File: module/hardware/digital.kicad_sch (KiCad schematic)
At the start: 41 parts, among them J10 Conn_01x03, J11 Conn_01x03, J12 Conn_01x03, J5 Conn_01x03_Male, J6 Conn_01x03_Male, J7 Conn_01x03, J8 Conn_01x03, J9 Conn_01x05_Male, SW2 SW_Push, U8 W25Q128JVS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

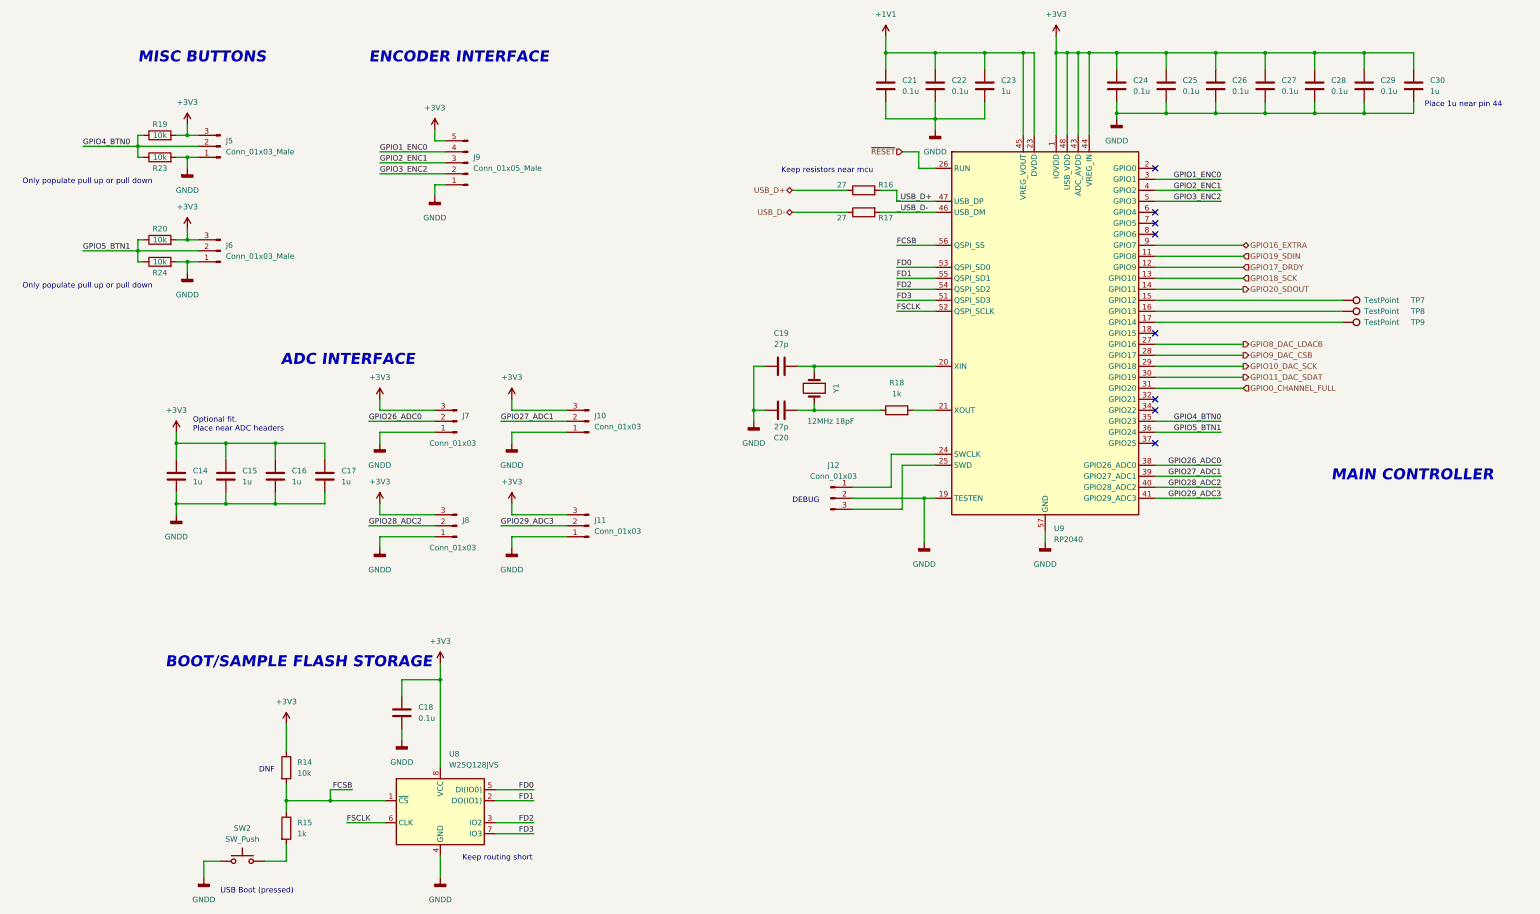
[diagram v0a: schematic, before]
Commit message: Add EXTRA1, btn debounce passives; Bump HW rev to 1.1
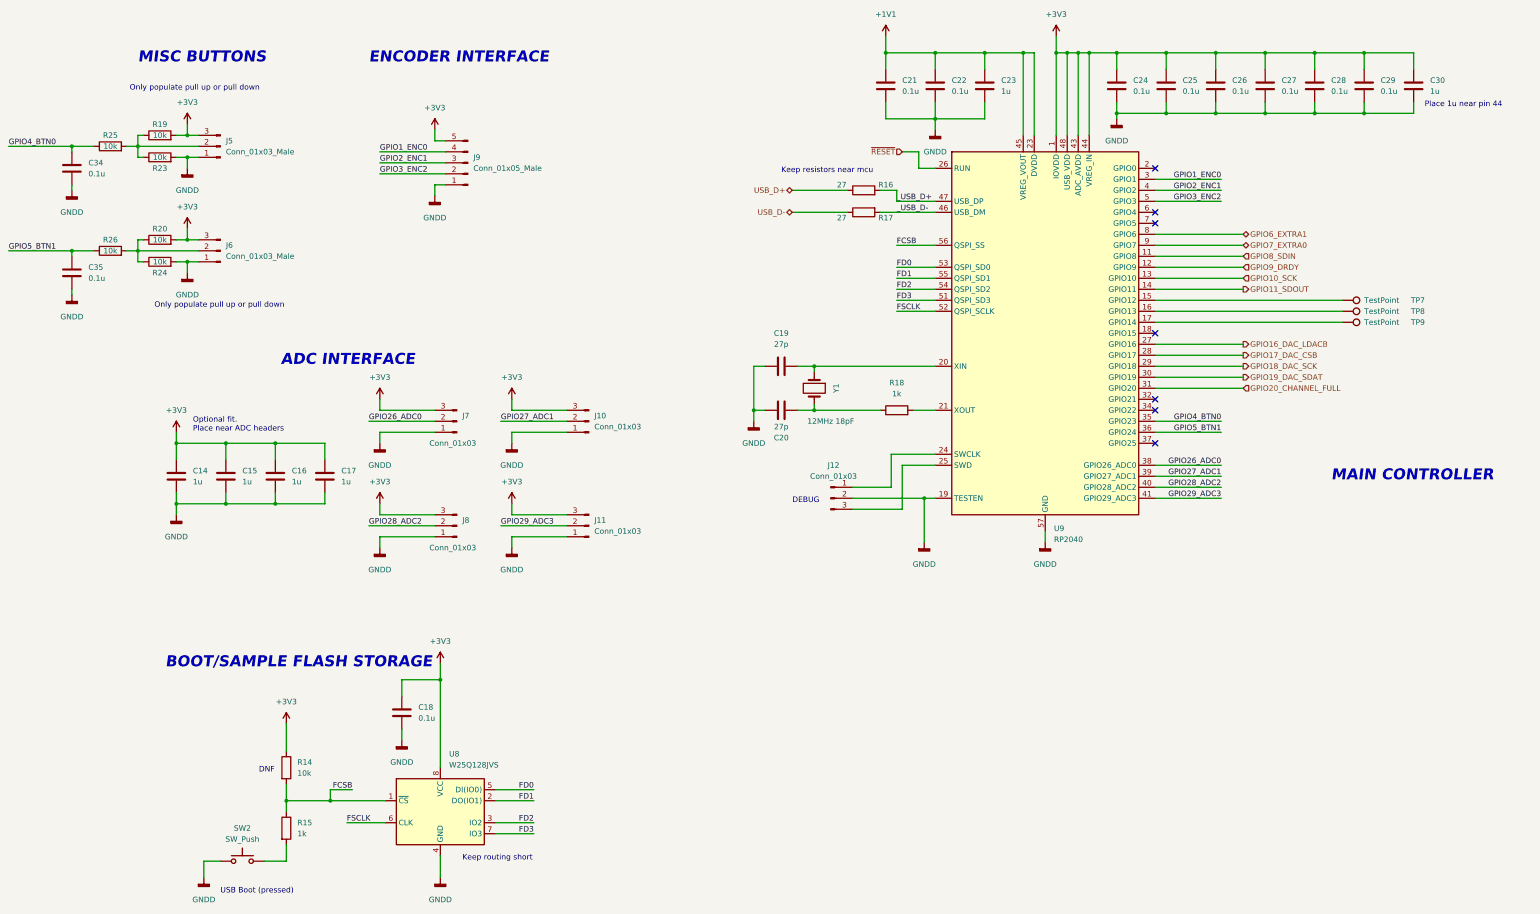
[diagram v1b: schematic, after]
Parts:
- added C34, C35: 0.1u, Capacitor_SMD:C_0603_1608Metric_Pad1.08x0.95mm_HandSolder, symbol Device:C
- added R25, R26: 10k, Resistor_SMD:R_0603_1608Metric_Pad0.98x0.95mm_HandSolder, symbol Device:R
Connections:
- net GNDD: now also C34.2, C35.2
- net GPIO4_BTN0: now also C34.1, R25.1; no longer J5.2 (Pin_2), R19.1, R23.1
- net GPIO5_BTN1: now also C35.1, R26.1; no longer J6.2 (Pin_2), R20.1, R24.1
- net GPIO6_EXTRA1: now reaches U9.8 (GPIO6)
- net GPIO0_CHANNEL_FULL renamed GPIO20_CHANNEL_FULL
- net GPIO10_DAC_SCK renamed GPIO18_DAC_SCK
- net GPIO11_DAC_SDAT renamed GPIO19_DAC_SDAT
- net GPIO16_EXTRA renamed GPIO7_EXTRA0
- net GPIO17_DRDY renamed GPIO9_DRDY
- net GPIO18_SCK renamed GPIO10_SCK
- net GPIO19_SDIN renamed GPIO8_SDIN
- net GPIO20_SDOUT renamed GPIO11_SDOUT
- net GPIO8_DAC_LDACB renamed GPIO16_DAC_LDACB
- net GPIO9_DAC_CSB renamed GPIO17_DAC_CSB
- new net: J5.2 (Pin_2), R19.1, R23.1, R25.2
- new net: J6.2 (Pin_2), R20.1, R24.1, R26.2
- no-connect marks 8 -> 7
